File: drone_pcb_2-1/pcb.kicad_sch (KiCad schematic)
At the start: 19 parts, among them IC1 A5936GLKTR-T, IC2 A5936GLKTR-T, IC3 A5936GLKTR-T, IC4 A5936GLKTR-T, J1 Conn_01x03, J2 Conn_01x03, J3 Conn_01x03, J4 Conn_01x03, U1 MPU-6050, U3 ESP32-WROOM-32

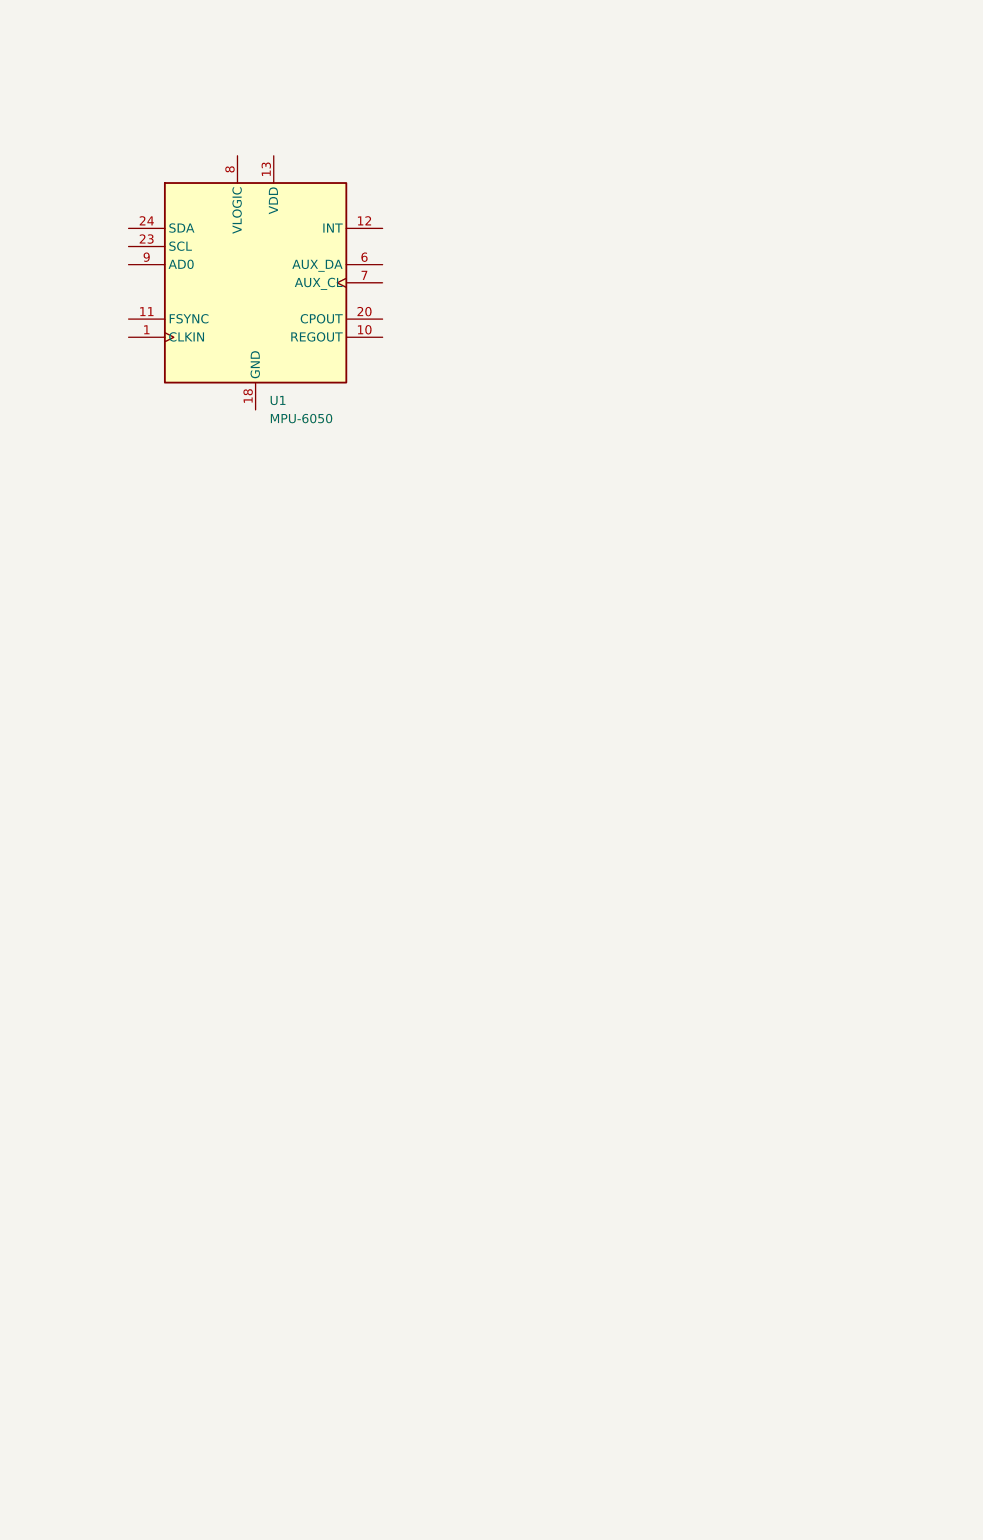
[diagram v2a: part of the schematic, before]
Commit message: add regulator + add bmp230
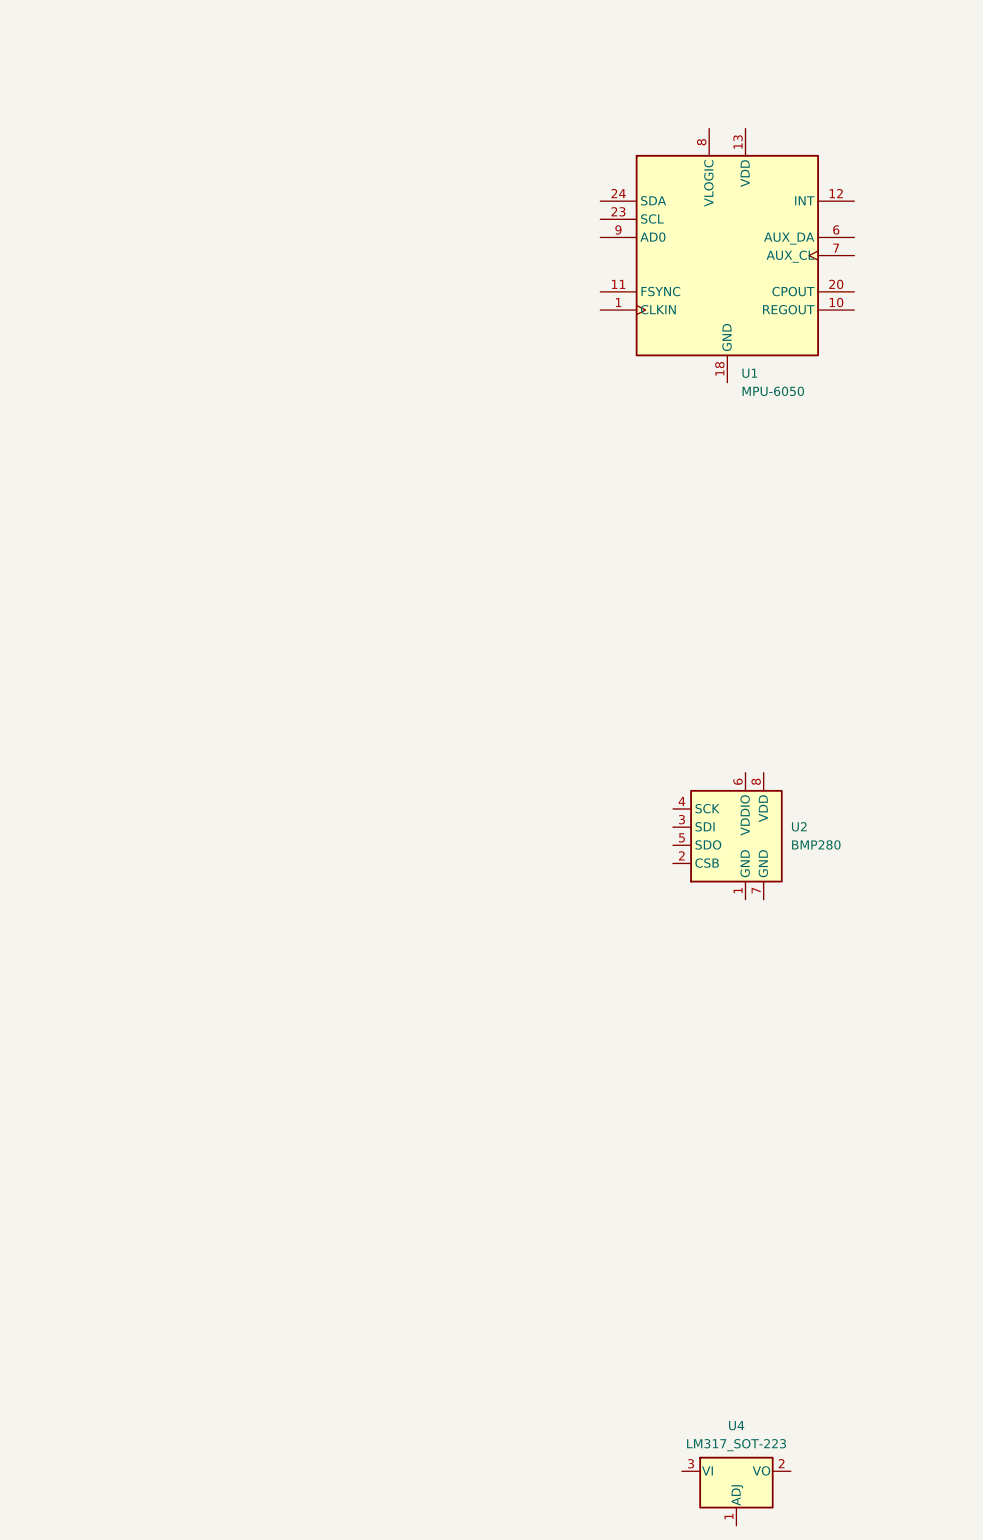
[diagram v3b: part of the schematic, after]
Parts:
- added U2: BMP280, Package_LGA:Bosch_LGA-8_2x2.5mm_P0.65mm_ClockwisePinNumbering, symbol Sensor_Pressure:BMP280
- added U4: LM317_SOT-223, Package_TO_SOT_SMD:SOT-223-3_TabPin2, symbol Regulator_Linear:LM317_SOT-223
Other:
- moved on the sheet: U1
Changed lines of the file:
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@@
+    )
+  )
+  (symbol (lib_id "Sensor_Pressure:BMP280") (at 227.33 149.86 0) (unit 1)
+    (in_bom yes) (on_board yes) (dnp no) (fields_autoplaced)
+    (property "Reference" "U2" (at 233.68 147.32 0)
+      (effects (font (size 1.27 1.27)) (justify left))
+    )
+    (property "Value" "BMP280" (at 233.68 149.86 0)
+      (effects (font (size 1.27 1.27)) (justify left))
+    )
+    (property "Footprint" "Package_LGA:Bosch_LGA-8_2x2.5mm_P0.65mm_ClockwisePinNumbering" (at 227.33 167.64 0)
+      (effects (font (size 1.27 1.27)) hide)
+    )
+    (property "Datasheet" "https://ae-bst.resource.bosch.com/media/_tech/media/datasheets/BST-BMP280-DS001.pdf" (at 227.33 149.86 0)
+      (effects (font (size 1.27 1.27)) hide)
+    )
+    (pin "1")
+    (pin "2")
+    (pin "3")
+    (pin "4")
+    (pin "5")
+    (pin "6")
+    (pin "7")
+    (pin "8")
+    (instances
+      (project "pcb"
+        (path "/86dd2ef4-708d-4533-9384-626d9620d24d"
+          (reference "U2") (unit 1)
+        )
+      )
     )
   )
@@
     )
   )
+  (symbol (lib_id "Regulator_Linear:LM317_SOT-223") (at 226.06 237.49 0) (unit 1)
+    (in_bom yes) (on_board yes) (dnp no) (fields_autoplaced)
+    (property "Reference" "U4" (at 226.06 231.14 0)
+      (effects (font (size 1.27 1.27)))
+    )
+    (property "Value" "LM317_SOT-223" (at 226.06 233.68 0)
+      (effects (font (size 1.27 1.27)))
+    )
+    (property "Footprint" "Package_TO_SOT_SMD:SOT-223-3_TabPin2" (at 226.06 231.14 0)
+      (effects (font (size 1.27 1.27) italic) hide)
+    )
+    (property "Datasheet" "http://www.ti.com/lit/ds/symlink/lm317.pdf" (at 226.06 237.49 0)
+      (effects (font (size 1.27 1.27)) hide)
+    )
+    (pin "1")
+    (pin "2")
+    (pin "3")
+    (instances
+      (project "pcb"
+        (path "/86dd2ef4-708d-4533-9384-626d9620d24d"
+          (reference "U4") (unit 1)
+        )
+      )
+    )
+  )
   (symbol (lib_id "power:GND") (at 349.25 104.14 0) (unit 1)
     (in_bom yes) (on_board yes) (dnp no) (fields_autoplaced)
@@
     )
   )
-  (symbol (lib_id "Sensor_Motion:MPU-6050") (at 158.75 71.12 0) (unit 1)
-    (in_bom yes) (on_board yes) (dnp no) (fields_autoplaced)
-    (property "Reference" "U1" (at 160.7059 87.63 0)
-      (effects (font (size 1.27 1.27)) (justify left))
-    )
-    (property "Value" "MPU-6050" (at 160.7059 90.17 0)
-      (effects (font (size 1.27 1.27)) (justify left))
-    )
-    (property "Footprint" "Sensor_Motion:InvenSense_QFN-24_4x4mm_P0.5mm" (at 158.75 91.44 0)
-      (effects (font (size 1.27 1.27)) hide)
-    )
-    (property "Datasheet" "https://invensense.tdk.com/wp-content/uploads/2015/02/MPU-6000-Datasheet1.pdf" (at 158.75 74.93 0)
-      (effects (font (size 1.27 1.27)) hide)
-    )
+  (symbol (lib_id "Sensor_Motion:MPU-6050") (at 224.79 67.31 0) (unit 1)
+    (in_bom yes) (on_board yes) (dnp no) (fields_autoplaced)
+    (property "Reference" "U1" (at 226.7459 83.82 0)
+      (effects (font (size 1.27 1.27)) (justify left))
+    )
+    (property "Value" "MPU-6050" (at 226.7459 86.36 0)
+      (effects (font (size 1.27 1.27)) (justify left))
+    )
+    (property "Footprint" "Sensor_Motion:InvenSense_QFN-24_4x4mm_P0.5mm" (at 224.79 87.63 0)
+      (effects (font (size 1.27 1.27)) hide)
+    )
+    (property "Datasheet" "https://invensense.tdk.com/wp-content/uploads/2015/02/MPU-6000-Datasheet1.pdf" (at 224.79 71.12 0)
+      (effects (font (size 1.27 1.27)) hide)
+    )
